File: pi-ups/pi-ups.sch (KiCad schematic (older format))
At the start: 16 parts, among them J1 USB_A, J2 USB_A, J3 USB_A, Q1 BC337, Q2 IRLM6244, Q3 IRLM6244, U1 DC-DC

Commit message: Minor update
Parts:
- U1: value DC-DC -> DC-DC Converter
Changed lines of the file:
@@
 P 4500 2450
 F 0 "U1" H 4500 2915 50  0000 C CNN
-F 1 "DC-DC" H 4500 2824 50  0000 C CNN
+F 1 "DC-DC Converter" H 4500 2824 50  0000 C CNN
 F 2 "" H 5050 2850 50  0001 C CNN
 F 3 "" H 5050 2850 50  0001 C CNN

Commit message: Minor update
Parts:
- R3: value 1K2 -> 1K5
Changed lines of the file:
@@
 P 3200 3600
 F 0 "R3" H 3270 3646 50  0000 L CNN
-F 1 "1K2" H 3270 3555 50  0000 L CNN
+F 1 "1K5" H 3270 3555 50  0000 L CNN
 F 2 "" V 3130 3600 50  0001 C CNN
 F 3 "~" H 3200 3600 50  0001 C CNN

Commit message: Add input/output labels
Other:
- note added: "Input\n"
- note added: "Output"
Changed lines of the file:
@@
 Text Label 5050 2350 0    50   ~ 0
 +5.5V
+Text Notes 1350 1200 0    59   ~ 12
+Input\n
+Text Notes 6500 1250 0    59   ~ 12
+Output
 $EndSCHEMATC

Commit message: Add different variants
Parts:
- added R?: 4K7, symbol Device:R
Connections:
- net GND: now also R?.2
- net at C1.1, D2.1 (K), D3.1 (K)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: now also R?.1
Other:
- moved on the sheet: C1
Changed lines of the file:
@@
 EESchema Schematic File Version 4
+LIBS:pi-ups-cache
 EELAYER 26 0
 EELAYER END
@@
 U 1 1 5C5411D5
 P 1550 1800
-F 0 "J1" H 1605 2267 50  0000 C CNN
-F 1 "USB_A" H 1605 2176 50  0000 C CNN
+F 0 "J1" H 1250 1850 50  0000 C CNN
+F 1 "USB_A" H 1200 1750 50  0000 C CNN
 F 2 "" H 1700 1750 50  0001 C CNN
 F 3 " ~" H 1700 1750 50  0001 C CNN
@@
 L Device:CP C1
 U 1 1 5C544DC4
-P 5950 2900
-F 0 "C1" H 6068 2946 50  0000 L CNN
-F 1 "1000µF/10V" V 5800 2700 50  0000 L CNN
-F 2 "" H 5988 2750 50  0001 C CNN
-F 3 "~" H 5950 2900 50  0001 C CNN
-	1    5950 2900
+P 5800 2800
+F 0 "C1" H 5918 2846 50  0000 L CNN
+F 1 "1000µF/10V" V 5650 2600 50  0000 L CNN
+F 2 "" H 5838 2650 50  0001 C CNN
+F 3 "~" H 5800 2800 50  0001 C CNN
+	1    5800 2800
 	1    0    0    -1
 $EndComp
@@
 	6700 2250 6700 2200
 Wire Wire Line
-	6400 1600 5950 1600
-Wire Wire Line
-	5950 1600 5950 1950
-Wire Wire Line
-	5950 2600 6400 2600
-Wire Wire Line
-	5600 1950 5950 1950
-Connection ~ 5950 1950
-Wire Wire Line
-	5950 1950 5950 2350
-Wire Wire Line
-	5600 2350 5950 2350
-Connection ~ 5950 2350
-Wire Wire Line
-	5950 2350 5950 2600
+	5600 1950 5800 1950
+Wire Wire Line
+	5800 1950 5800 2350
+Wire Wire Line
+	5600 2350 5800 2350
+Connection ~ 5800 2350
 $Comp
 L power:GND #PWR09
 U 1 1 5C548167
-P 5950 3250
-F 0 "#PWR09" H 5950 3000 50  0001 C CNN
-F 1 "GND" H 5955 3077 50  0000 C CNN
-F 2 "" H 5950 3250 50  0001 C CNN
-F 3 "" H 5950 3250 50  0001 C CNN
-	1    5950 3250
-	1    0    0    -1
-$EndComp
-Wire Wire Line
-	5950 3250 5950 3050
-Wire Wire Line
-	5950 2750 5950 2600
-Connection ~ 5950 2600
+P 5800 3250
+F 0 "#PWR09" H 5800 3000 50  0001 C CNN
+F 1 "GND" H 5805 3077 50  0000 C CNN
+F 2 "" H 5800 3250 50  0001 C CNN
+F 3 "" H 5800 3250 50  0001 C CNN
+	1    5800 3250
+	1    0    0    -1
+$EndComp
+Wire Wire Line
+	5800 3250 5800 3200
 $Comp
 L microfarad-de:DC-DC U1
@@
 Text Label 5050 2350 0    50   ~ 0
 +5.5V
-Text Notes 1350 1200 0    59   ~ 12
+Text Notes 1350 1250 0    59   ~ 12
 Input\n
 Text Notes 6500 1250 0    59   ~ 12
 Output
+$Comp
+L Device:R R?
+U 1 1 5C543498
+P 6100 2800
+F 0 "R?" H 6170 2846 50  0000 L CNN
+F 1 "4K7" H 6170 2755 50  0000 L CNN
+F 2 "" V 6030 2800 50  0001 C CNN
+F 3 "~" H 6100 2800 50  0001 C CNN
+	1    6100 2800
+	1    0    0    -1
+$EndComp
+Wire Wire Line
+	6100 2950 6100 3200
+Wire Wire Line
+	6100 3200 5800 3200
+Connection ~ 5800 3200
+Wire Wire Line
+	5800 3200 5800 2950
+Wire Wire Line
+	5800 2350 5800 2650
+Wire Wire Line
+	6400 1600 6300 1600
+Wire Wire Line
+	6300 1600 6300 2350
+Wire Wire Line
+	6300 2600 6400 2600
+Wire Wire Line
+	5800 2350 6100 2350
+Connection ~ 6300 2350
+Wire Wire Line
+	6300 2350 6300 2600
+Wire Wire Line
+	6100 2650 6100 2350
+Connection ~ 6100 2350
+Wire Wire Line
+	6100 2350 6300 2350
 $EndSCHEMATC

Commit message: Beautify
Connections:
- net +BATT: now reaches BT1.1 (+), R1.2, R4.1, U1.~ (OUT-)
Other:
- moved on the sheet: R?
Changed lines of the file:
@@
 EESchema Schematic File Version 4
 LIBS:pi-ups-cache
+LIBS:pi-ups-high-cache
 EELAYER 26 0
 EELAYER END
@@
 $EndComp
 $Comp
-L power:+5V #PWR02
-U 1 1 5C542401
-P 2000 1500
-F 0 "#PWR02" H 2000 1350 50  0001 C CNN
-F 1 "+5V" H 2015 1673 50  0000 C CNN
-F 2 "" H 2000 1500 50  0001 C CNN
-F 3 "" H 2000 1500 50  0001 C CNN
-	1    2000 1500
-	1    0    0    -1
-$EndComp
-$Comp
 L power:GND #PWR01
 U 1 1 5C542562
@@
 Wire Wire Line
 	1550 2350 1550 2200
-Wire Wire Line
-	1850 1600 2000 1600
-Wire Wire Line
-	2000 1600 2000 1500
 $Comp
 L power:+5V #PWR03
@@
 $EndComp
 Wire Wire Line
-	2600 1500 2600 1650
+	2600 1500 2600 1600
 Wire Wire Line
 	2600 2000 2600 1950
-Wire Wire Line
-	2600 2300 2600 2350
 $Comp
 L power:GND #PWR07
@@
 Wire Wire Line
 	2600 3800 2600 3300
-Connection ~ 2600 2350
-Wire Wire Line
-	2600 2350 2600 2900
 $Comp
 L Device:R R3
@@
 $EndComp
 $Comp
-L power:+5V #PWR05
-U 1 1 5C544A89
-P 3200 2900
-F 0 "#PWR05" H 3200 2750 50  0001 C CNN
-F 1 "+5V" H 3215 3073 50  0000 C CNN
-F 2 "" H 3200 2900 50  0001 C CNN
-F 3 "" H 3200 2900 50  0001 C CNN
-	1    3200 2900
-	1    0    0    -1
-$EndComp
-$Comp
 L Device:CP C1
 U 1 1 5C544DC4
 P 5800 2800
-F 0 "C1" H 5918 2846 50  0000 L CNN
+F 0 "C1" H 5700 2650 50  0000 L CNN
 F 1 "1000µF/10V" V 5650 2600 50  0000 L CNN
 F 2 "" H 5838 2650 50  0001 C CNN
@@
 Wire Wire Line
 	5000 2350 5300 2350
-$Comp
-L power:+5V #PWR08
-U 1 1 5C546347
-P 5200 1500
-F 0 "#PWR08" H 5200 1350 50  0001 C CNN
-F 1 "+5V" H 5215 1673 50  0000 C CNN
-F 2 "" H 5200 1500 50  0001 C CNN
-F 3 "" H 5200 1500 50  0001 C CNN
-	1    5200 1500
-	1    0    0    -1
-$EndComp
 Wire Wire Line
 	5300 1950 5200 1950
-Wire Wire Line
-	5200 1950 5200 1500
 $Comp
 L power:GND #PWR010
@@
 $EndComp
 Wire Wire Line
-	5800 3250 5800 3200
+	5800 3250 5800 3050
 $Comp
 L microfarad-de:DC-DC U1
@@
 $EndComp
 Wire Wire Line
-	2600 2350 3550 2350
-Wire Wire Line
-	3200 2950 3200 2900
-Wire Wire Line
 	3550 2750 3550 2350
-Connection ~ 3550 2350
 Wire Wire Line
 	3550 2350 4000 2350
@@
 L Device:R R?
 U 1 1 5C543498
-P 6100 2800
-F 0 "R?" H 6170 2846 50  0000 L CNN
-F 1 "4K7" H 6170 2755 50  0000 L CNN
-F 2 "" V 6030 2800 50  0001 C CNN
-F 3 "~" H 6100 2800 50  0001 C CNN
-	1    6100 2800
-	1    0    0    -1
-$EndComp
-Wire Wire Line
-	6100 2950 6100 3200
-Wire Wire Line
-	6100 3200 5800 3200
-Connection ~ 5800 3200
-Wire Wire Line
-	5800 3200 5800 2950
-Wire Wire Line
-	5800 2350 5800 2650
+P 6050 2800
+F 0 "R?" H 6120 2846 50  0000 L CNN
+F 1 "4K7" H 6120 2755 50  0000 L CNN
+F 2 "" V 5980 2800 50  0001 C CNN
+F 3 "~" H 6050 2800 50  0001 C CNN
+	1    6050 2800
+	1    0    0    -1
+$EndComp
+Wire Wire Line
+	6050 2950 6050 3050
+Wire Wire Line
+	6050 3050 5800 3050
+Connection ~ 5800 3050
+Wire Wire Line
+	5800 3050 5800 2950
+Wire Wire Line
+	5800 2350 5800 2550
 Wire Wire Line
 	6400 1600 6300 1600
@@
 Wire Wire Line
 	6300 2600 6400 2600
-Wire Wire Line
-	5800 2350 6100 2350
 Connection ~ 6300 2350
 Wire Wire Line
 	6300 2350 6300 2600
 Wire Wire Line
-	6100 2650 6100 2350
-Connection ~ 6100 2350
-Wire Wire Line
-	6100 2350 6300 2350
+	5800 2350 6300 2350
+Wire Wire Line
+	6050 2650 6050 2550
+Wire Wire Line
+	6050 2550 5800 2550
+Connection ~ 5800 2550
+Wire Wire Line
+	5800 2550 5800 2650
+Wire Wire Line
+	1850 1600 2600 1600
+Connection ~ 2600 1600
+Wire Wire Line
+	2600 1600 2600 1650
+Wire Wire Line
+	5200 1600 5200 1950
+$Comp
+L power:+BATT #PWR?
+U 1 1 5C557336
+P 2800 2600
+F 0 "#PWR?" H 2800 2450 50  0001 C CNN
+F 1 "+BATT" H 2815 2773 50  0000 C CNN
+F 2 "" H 2800 2600 50  0001 C CNN
+F 3 "" H 2800 2600 50  0001 C CNN
+	1    2800 2600
+	1    0    0    -1
+$EndComp
+Wire Wire Line
+	2600 2300 2600 2750
+Wire Wire Line
+	2800 2600 2800 2750
+Wire Wire Line
+	2800 2750 2600 2750
+Connection ~ 2600 2750
+Wire Wire Line
+	2600 2750 2600 2900
+$Comp
+L power:+BATT #PWR?
+U 1 1 5C558370
+P 3550 2200
+F 0 "#PWR?" H 3550 2050 50  0001 C CNN
+F 1 "+BATT" H 3565 2373 50  0000 C CNN
+F 2 "" H 3550 2200 50  0001 C CNN
+F 3 "" H 3550 2200 50  0001 C CNN
+	1    3550 2200
+	1    0    0    -1
+$EndComp
+Wire Wire Line
+	3550 2350 3550 2200
+Connection ~ 3550 2350
+Wire Wire Line
+	3200 1600 3200 2950
+Wire Wire Line
+	2600 1600 3200 1600
+Connection ~ 3200 1600
+Wire Wire Line
+	3200 1600 5200 1600
 $EndSCHEMATC

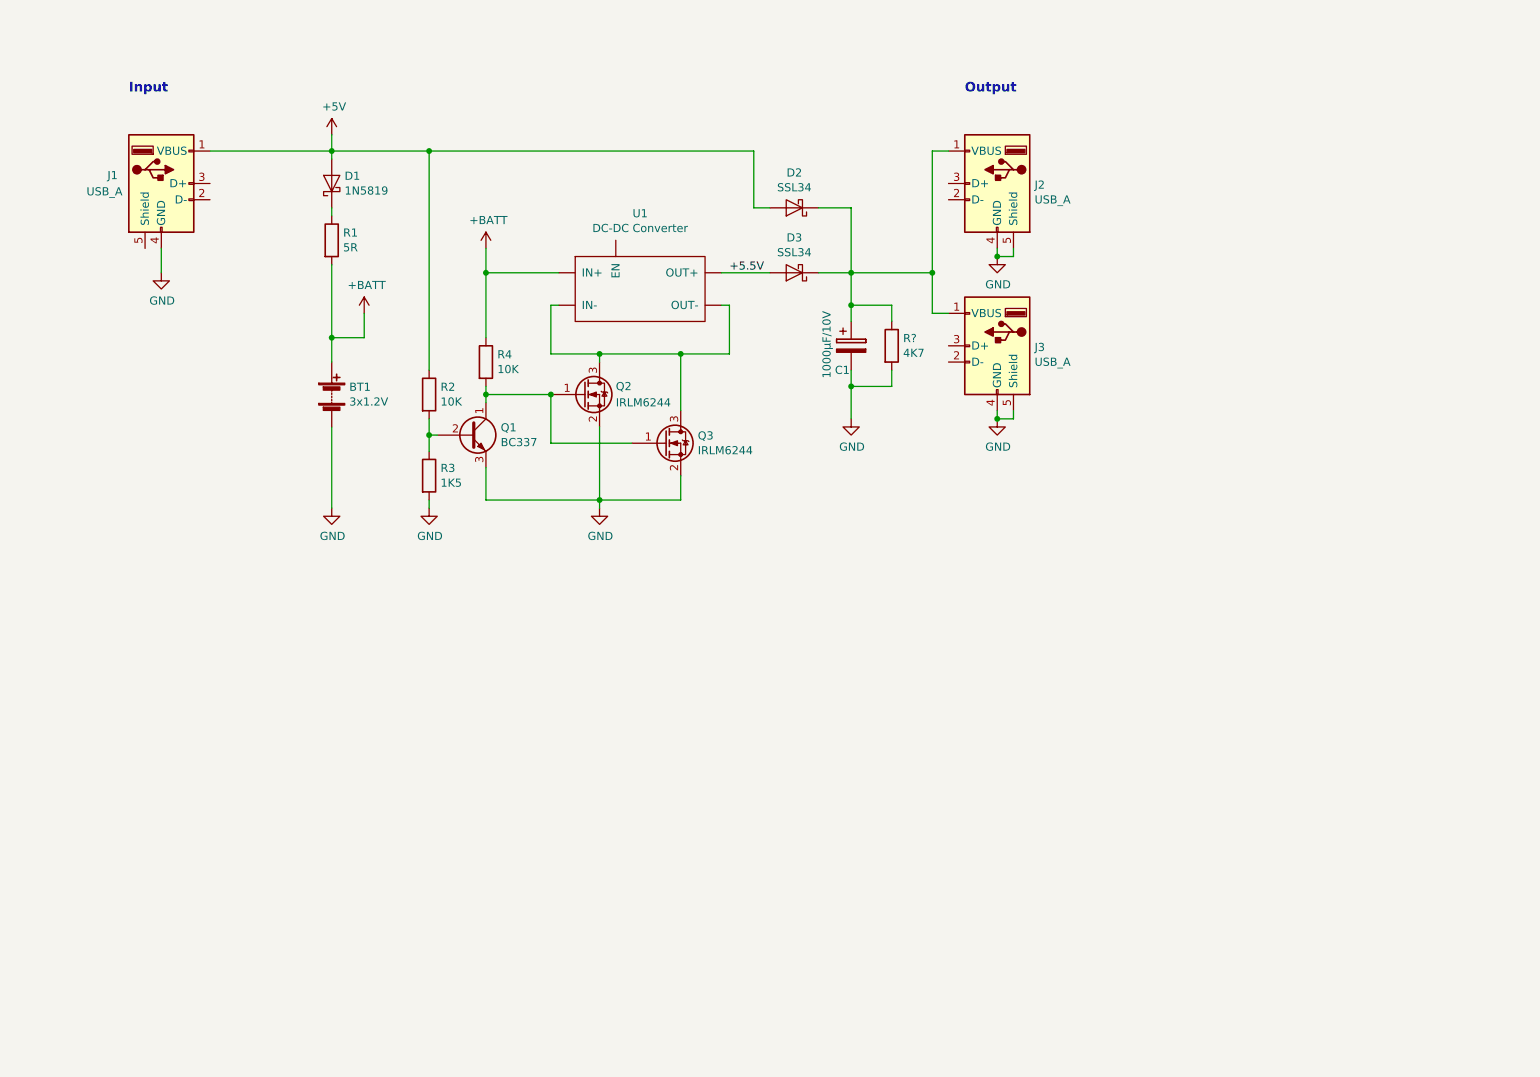
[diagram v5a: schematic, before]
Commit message: Implementing pi-ups schematic
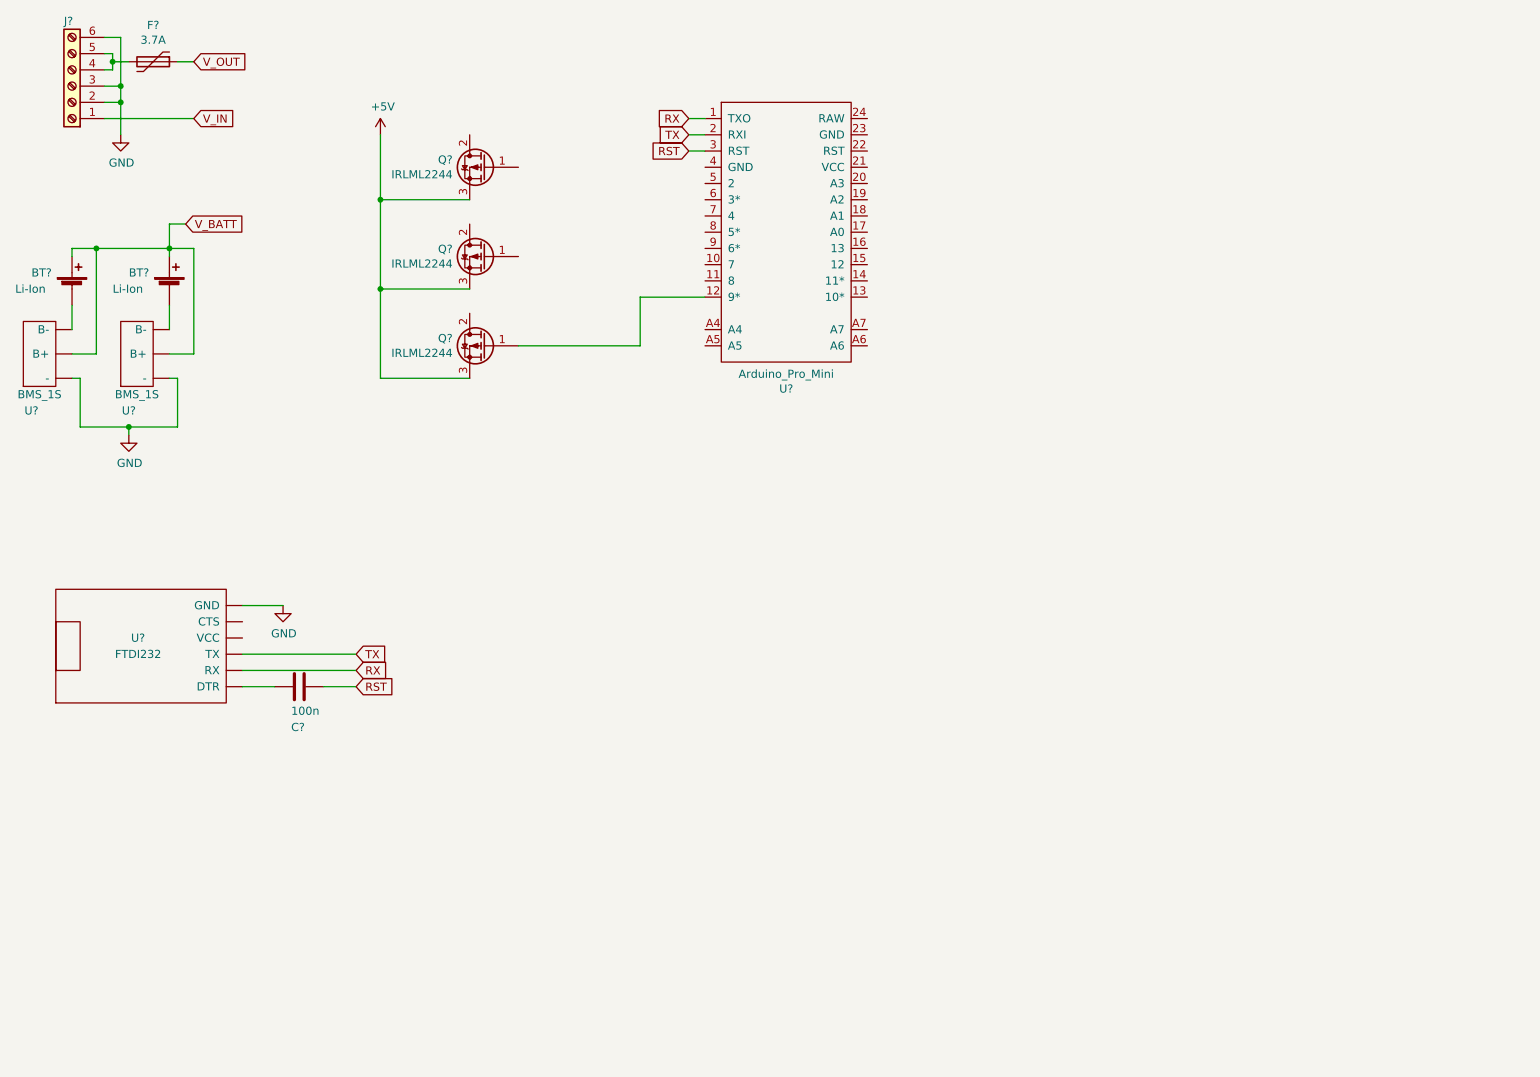
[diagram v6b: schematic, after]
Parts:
- removed BT1: 3x1.2V, symbol Device:Battery
- removed C1: 1000µF/10V, symbol Device:CP
- removed D1: 1N5819, symbol Device:D_Schottky
- removed D2, D3: SSL34, symbol Device:D_Schottky
- removed J1, J2, J3: USB_A, symbol Connector:USB_A
- removed Q1: BC337, symbol Device:Q_NPN_CBE
- removed Q2, Q3: IRLM6244, symbol Device:Q_NMOS_GSD
- removed R1: 5R, symbol Device:R
- removed R2, R4: 10K, symbol Device:R
- removed R3: 1K5, symbol Device:R
- removed R?: 4K7, symbol Device:R
- removed U1: DC-DC Converter, symbol microfarad-de:DC-DC
- added BT? (x2): Li-Ion, symbol Device:Battery_Cell
- added C?: 100n, symbol Device:C
- added F?: 3.7A, symbol Device:Polyfuse
- added J?: (no value), symbol Connector:Screw_Terminal_01x06
- added Q? (x3): IRLML2244, symbol Device:Q_PMOS_GDS
- added U?: Arduino_Pro_Mini, symbol microfarad-de:Arduino_Pro_Mini
- added U?: FTDI232, symbol microfarad-de:FTDI232
- added U? (x2): BMS_1S, symbol microfarad-de:BMS_1S
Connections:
- net +5V: now also Q?.3 (S), Q?.3 (S), Q?.3 (S)
- net GND: now also J?.2 (Pin_2), J?.3 (Pin_3), J?.6 (Pin_6), U?.~ (B-), U?.~ (B-), U?.~ (VCC)
- new net: Q?.1 (G), U?.12 (9*)
- new net: C?.1, U?.~ (VCC)
- new net: F?.2, J?.4 (Pin_4), J?.5 (Pin_5)
- new net: BT?.2 (-), U?.~ (B-) (x2)
- new net RST: C?.2, U?.3 (RST)
- new net RX: U?.1 (TXO), U?.~ (VCC)
- new net TX: U?.2 (RXI), U?.~ (VCC)
- new net V_BATT: BT?.1 (+), BT?.1 (+), U?.~ (B-), U?.~ (B-)
- new net V_IN: J?.1 (Pin_1)
- new net V_OUT: F?.1
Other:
- note removed: "Input\n"
- note removed: "Output"

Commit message: pi-ups: finalized initial version
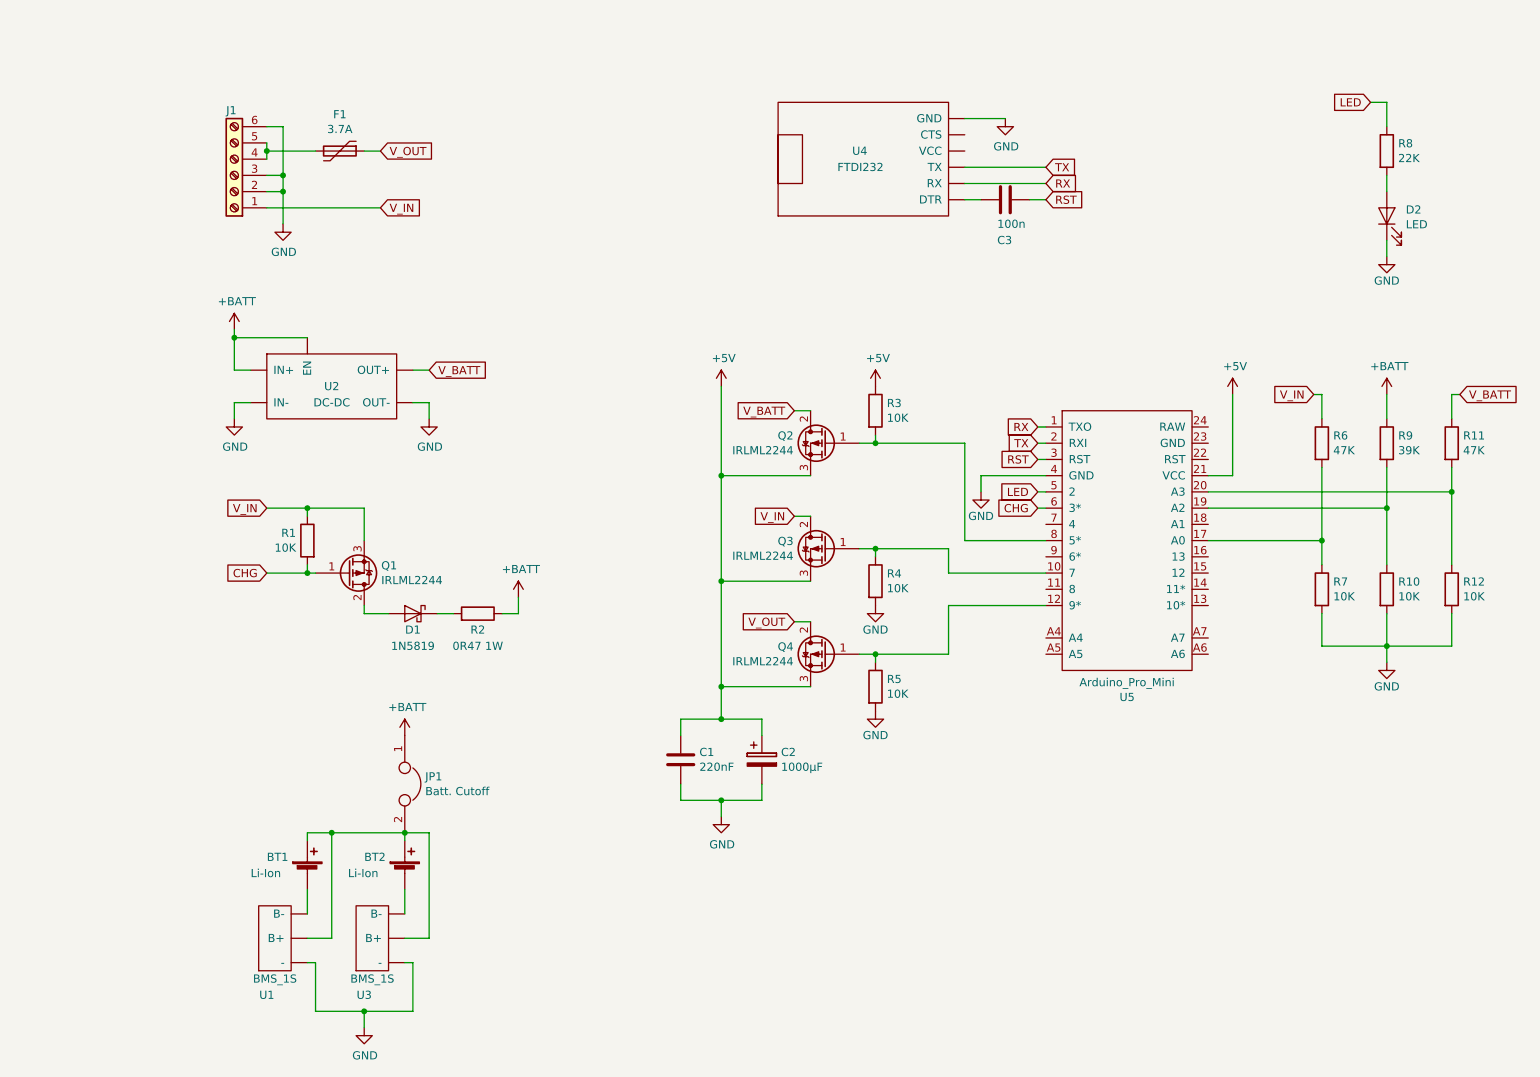
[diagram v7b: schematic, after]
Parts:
- added C1: 220nF, symbol Device:C
- added C2: 1000µF, symbol Device:CP
- added D1: 1N5819, Diode_THT:D_DO-41_SOD81_P10.16mm_Horizontal, symbol Diode:1N5819
- added D2: LED, symbol Device:LED
- added JP1: Batt. Cutoff, symbol Device:Jumper
- added Q1: IRLML2244, symbol Device:Q_PMOS_GDS
- added R1, R10, R12, R3, R4, R5, R7: 10K, symbol Device:R
- added R11, R6: 47K, symbol Device:R
- added R2: 0R47 1W, symbol Device:R
- added R8: 22K, symbol Device:R
- added R9: 39K, symbol Device:R
- added U2: DC-DC, symbol microfarad-de:DC-DC
- gave numbers to parts that had none: 12
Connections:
- net +5V: now also U5.21 (VCC), C1.1, C2.1, R3.1
- net GND: now also U5.4 (GND), C1.2, C2.2, D2.1 (K), R10.2, R12.2, R4.2, R5.2, R7.2, U2.~ (OUT-)
- net V_BATT: now also Q2.2 (D), R11.1, U2.~ (OUT-); no longer BT1.1 (+), BT2.1 (+), U1.~ (B-), U3.~ (B-)
- net V_IN: now also Q3.2 (D), Q1.3 (S), R1.1, R6.1
- net V_OUT: now also Q4.2 (D)
- net at U5.10 (7): now also Q3.1 (G), R4.1
- net at Q4.1 (G), U5.12 (9*): now also R5.1
- net at U5.17 (A0): now also R6.2, R7.1
- net at U5.19 (A2): now also R10.1, R9.2
- net at U5.20 (A3): now also R11.2, R12.1
- net LED: now reaches U5.5 (2)
- net LED: now also R8.1
- net CHG: now reaches U5.6 (3*)
- net CHG: now also Q1.1 (G), R1.2
- net at U5.8 (5*): now also Q2.1 (G), R3.2
- new net: BT1.1 (+), BT2.1 (+), JP1.2, U1.~ (B-), U3.~ (B-)
- new net: D2.2 (A), R8.2
- new net: D1.2 (A), Q1.2 (D)
- new net: D1.1 (K), R2.2
- new net +BATT: JP1.1, R2.1, R9.1, U2.~ (OUT-)
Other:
- moved on the sheet: BT1, BT2, C3, F1, J1, Q2, Q3, Q4, U1, U3, U4, U5
